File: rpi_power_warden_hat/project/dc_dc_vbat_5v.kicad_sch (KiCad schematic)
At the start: 15 parts, among them U4 TPS563200

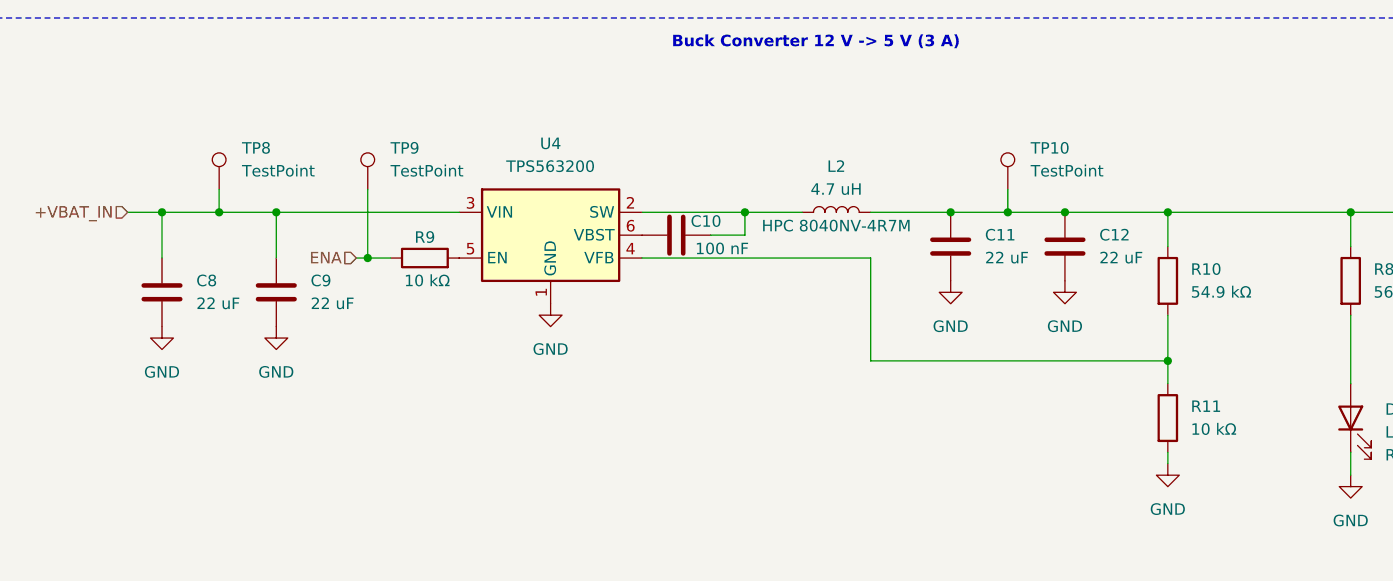
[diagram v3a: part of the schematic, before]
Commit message: add RPi HAT eeprom to schematic
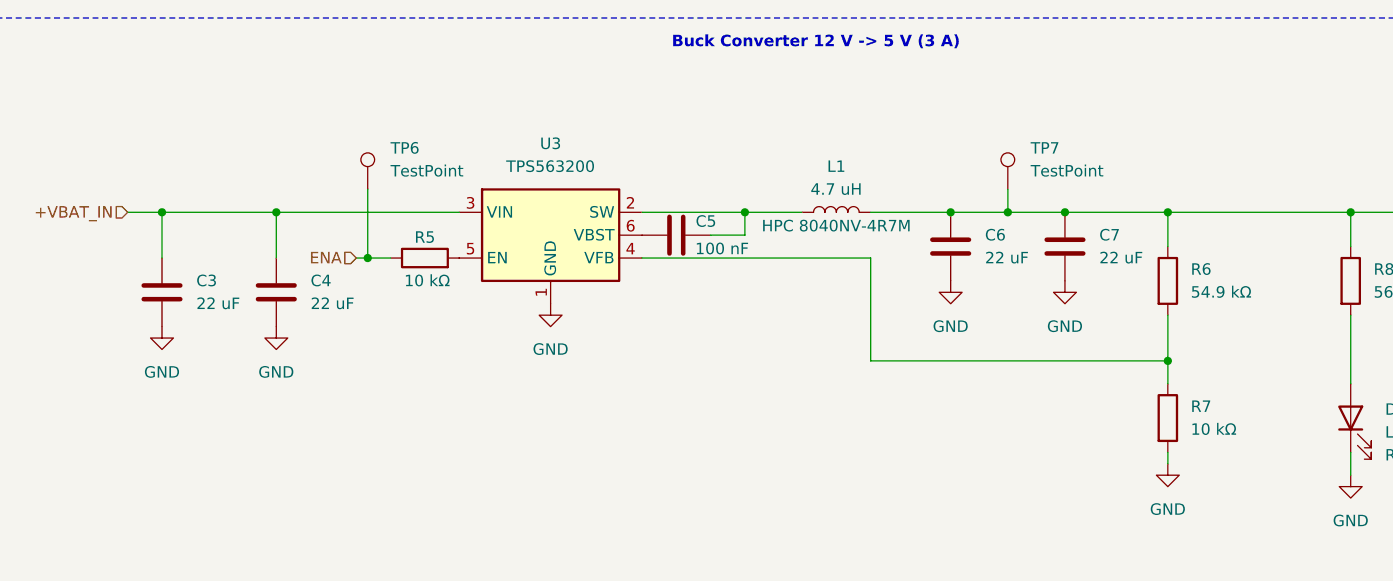
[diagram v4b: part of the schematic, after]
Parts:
- removed TP8: TestPoint, TestPoint:TestPoint_Pad_D2.5mm, symbol Connector:TestPoint
- renumbered C8 to C3, C9 to C4, C10 to C5, C11 to C6, C12 to C7, L2 to L1, R9 to R5, R10 to R6, R11 to R7, TP9 to TP6, TP10 to TP7, U4 to U3
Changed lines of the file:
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@@
 	)
 	(junction
-		(at 91.44 85.09)
-		(diameter 0)
-		(color 0 0 0 0)
-	)
-	(junction
 		(at 107.95 90.17)
 		(diameter 0)
@@
 	(wire
 		(pts
-			(xy 91.44 85.09) (xy 97.79 85.09)
+			(xy 85.09 85.09) (xy 97.79 85.09)
 		)
 		(stroke
@@
 	(wire
 		(pts
-			(xy 91.44 82.55) (xy 91.44 85.09)
-		)
-		(stroke
-			(width 0)
-			(type default)
-		)
-	)
-	(wire
-		(pts
 			(xy 217.17 85.09) (xy 217.17 88.9)
 		)
@@
 	(wire
 		(pts
-			(xy 85.09 85.09) (xy 91.44 85.09)
-		)
-		(stroke
-			(width 0)
-			(type default)
-		)
-	)
-	(wire
-		(pts
 			(xy 138.43 90.17) (xy 163.83 90.17)
 		)
@@
 		(dnp no)
 		(fields_autoplaced yes)
-		(property "Reference" "C8"
+		(property "Reference" "C3"
 			(at 88.9 92.7099 0)
 			(effects
@@
 		(dnp no)
 		(fields_autoplaced yes)
-		(property "Reference" "#PWR24"
+		(property "Reference" "#PWR17"
 			(at 172.72 99.06 0)
 			(effects
@@
 		(dnp no)
 		(fields_autoplaced yes)
-		(property "Reference" "C12"
+		(property "Reference" "C7"
 			(at 189.23 87.6299 0)
 			(effects
@@
 		(dnp no)
 		(fields_autoplaced yes)
-		(property "Reference" "R11"
+		(property "Reference" "R7"
 			(at 199.39 106.6799 0)
 			(effects
@@
 		(dnp no)
 		(fields_autoplaced yes)
-		(property "Reference" "#PWR23"
+		(property "Reference" "#PWR16"
 			(at 128.27 101.6 0)
 			(effects
@@
 		(dnp no)
 		(fields_autoplaced yes)
-		(property "Reference" "TP10"
+		(property "Reference" "TP7"
 			(at 181.61 77.9779 0)
 			(effects
@@
 		(dnp no)
 		(fields_autoplaced yes)
-		(property "Reference" "#PWR25"
+		(property "Reference" "#PWR18"
 			(at 185.42 99.06 0)
 			(effects
@@
 		(on_board yes)
 		(dnp no)
-		(property "Reference" "C10"
+		(property "Reference" "C5"
 			(at 145.542 86.106 90)
 			(effects
@@
 		(dnp no)
 		(fields_autoplaced yes)
-		(property "Reference" "#PWR22"
+		(property "Reference" "#PWR15"
 			(at 97.79 104.14 0)
 			(effects
@@
 	)
 	(symbol
-		(lib_id "Connector:TestPoint")
-		(at 91.44 82.55 0)
-		(unit 1)
-		(exclude_from_sim no)
-		(in_bom yes)
-		(on_board yes)
-		(dnp no)
-		(fields_autoplaced yes)
-		(property "Reference" "TP8"
-			(at 93.98 77.9779 0)
-			(effects
-				(font
-					(size 1.27 1.27)
-				)
-				(justify left)
-			)
-		)
-		(property "Value" "TestPoint"
-			(at 93.98 80.5179 0)
-			(effects
-				(font
-					(size 1.27 1.27)
-				)
-				(justify left)
-			)
-		)
-		(property "Footprint" "TestPoint:TestPoint_Pad_D2.5mm"
-			(at 96.52 82.55 0)
-			(effects
-				(font
-					(size 1.27 1.27)
-				)
-				(hide yes)
-			)
-		)
-		(property "Datasheet" "~"
-			(at 96.52 82.55 0)
-			(effects
-				(font
-					(size 1.27 1.27)
-				)
-				(hide yes)
-			)
-		)
-		(property "Description" "test point"
-			(at 91.44 82.55 0)
-			(effects
-				(font
-					(size 1.27 1.27)
-				)
-				(hide yes)
-			)
-		)
-		(pin "1"
-		)
-		(instances
-			(project "rpi_power_warden_hat"
-				(path "/8692c5de-a943-41e8-8e29-f6c5e99cda34/5bbc6f2d-46db-4213-8835-1ada71ba8330"
-					(reference "TP5")
-					(unit 1)
-				)
-				(path "/8692c5de-a943-41e8-8e29-f6c5e99cda34/cc58a92a-1392-4aa4-91cc-7a70ded8904f"
-					(reference "TP8")
-					(unit 1)
-				)
-			)
-		)
-	)
-	(symbol
 		(lib_id "Device:LED")
 		(at 217.17 107.95 90)
@@
 		(dnp no)
 		(fields_autoplaced yes)
-		(property "Reference" "TP9"
+		(property "Reference" "TP6"
 			(at 110.49 77.9779 0)
 			(effects
@@
 		(dnp no)
 		(fields_autoplaced yes)
-		(property "Reference" "#PWR21"
+		(property "Reference" "#PWR14"
 			(at 85.09 104.14 0)
 			(effects
@@
 		(dnp no)
 		(fields_autoplaced yes)
-		(property "Reference" "C9"
+		(property "Reference" "C4"
 			(at 101.6 92.7099 0)
 			(effects
@@
 		(dnp no)
 		(fields_autoplaced yes)
-		(property "Reference" "#PWR26"
+		(property "Reference" "#PWR19"
 			(at 196.85 119.38 0)
 			(effects
@@
 		(dnp no)
 		(fields_autoplaced yes)
-		(property "Reference" "U4"
+		(property "Reference" "U3"
 			(at 128.27 77.47 0)
 			(effects
@@
 		(dnp no)
 		(fields_autoplaced yes)
-		(property "Reference" "C11"
+		(property "Reference" "C6"
 			(at 176.53 87.6299 0)
 			(effects
@@
 		(dnp no)
 		(fields_autoplaced yes)
-		(property "Reference" "R10"
+		(property "Reference" "R6"
 			(at 199.39 91.4399 0)
 			(effects
@@
 		(on_board yes)
 		(dnp no)
-		(property "Reference" "R9"
+		(property "Reference" "R5"
 			(at 114.3 87.884 90)
 			(effects
@@
 		(on_board yes)
 		(dnp no)
-		(property "Reference" "L2"
+		(property "Reference" "L1"
 			(at 160.02 80.01 90)
 			(effects

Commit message: re-annotate schematic
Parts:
- renumbered C3 to C4, C4 to C5, C5 to C6, C6 to C7, C7 to C8, R7 to R10, R8 to R11, R5 to R8, R6 to R9, U3 to U4

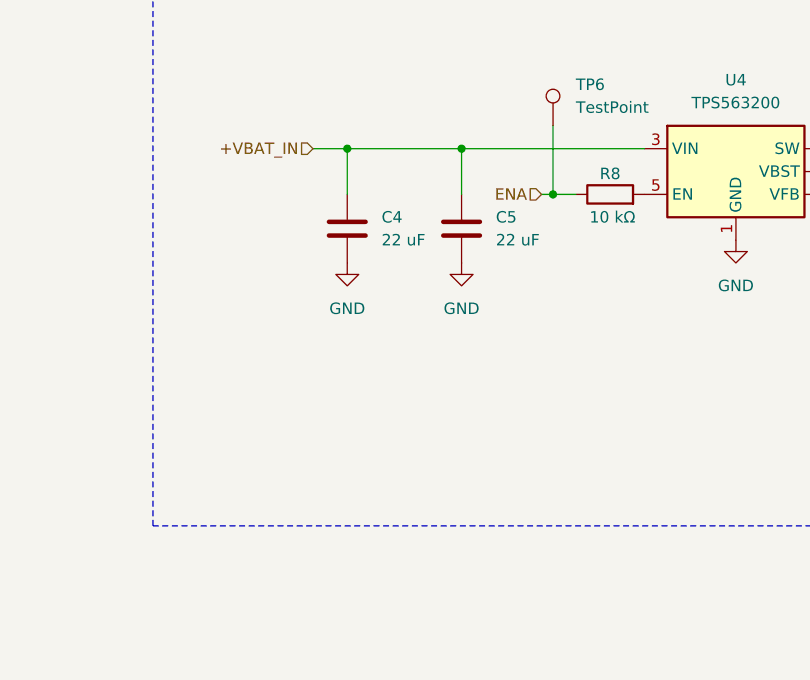
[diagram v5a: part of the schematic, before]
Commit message: add and gate in swiched power supplies enable
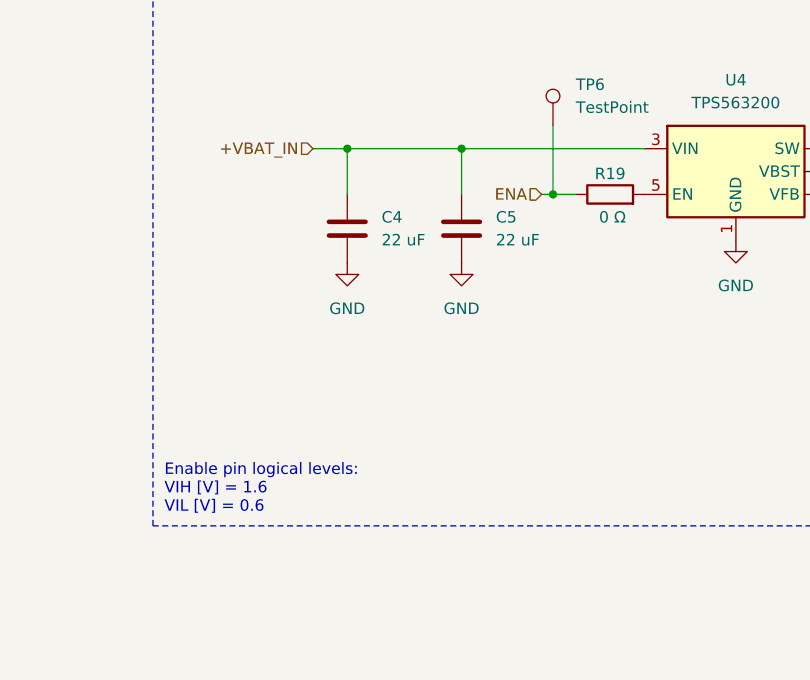
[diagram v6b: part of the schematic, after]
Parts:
- removed R8: 10 kΩ, Resistor_SMD:R_0603_1608Metric_Pad0.98x0.95mm_HandSolder, symbol Device:R
- added R19: 0 Ω, Resistor_SMD:R_0603_1608Metric_Pad0.98x0.95mm_HandSolder, symbol Device:R
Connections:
- net ENA: now also R19.1
- net at U4.5 (EN): now also R19.2
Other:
- note added: "Enable pin logical levels: VIH [V] = 1.6 VIL [V] = 0.6"
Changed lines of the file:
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@@
+		)
+	)
+	(text "Enable pin logical levels:\nVIH [V] = 1.6\nVIL [V] = 0.6"
+		(exclude_from_sim no)
+		(at 64.77 122.936 0)
+		(effects
+			(font
+				(size 1.27 1.27)
+			)
+			(justify left)
 		)
 	)
@@
 	)
 	(symbol
+		(lib_id "Device:R")
+		(at 114.3 90.17 90)
+		(unit 1)
+		(exclude_from_sim no)
+		(in_bom yes)
+		(on_board yes)
+		(dnp no)
+		(property "Reference" "R19"
+			(at 114.3 87.884 90)
+			(effects
+				(font
+					(size 1.27 1.27)
+				)
+			)
+		)
+		(property "Value" "0 Ω"
+			(at 114.554 92.71 90)
+			(effects
+				(font
+					(size 1.27 1.27)
+				)
+			)
+		)
+		(property "Footprint" "Resistor_SMD:R_0603_1608Metric_Pad0.98x0.95mm_HandSolder"
+			(at 114.3 91.948 90)
+			(effects
+				(font
+					(size 1.27 1.27)
+				)
+				(hide yes)
+			)
+		)
+		(property "Datasheet" "~"
+			(at 114.3 90.17 0)
+			(effects
+				(font
+					(size 1.27 1.27)
+				)
+				(hide yes)
+			)
+		)
+		(property "Description" "RES SMD 0 OHM JUMPER 1/10W 0603"
+			(at 114.3 90.17 0)
+			(effects
+				(font
+					(size 1.27 1.27)
+				)
+				(hide yes)
+			)
+		)
+		(property "mpn" "ERJ-3GEY0R00V"
+			(at 114.3 90.17 0)
+			(effects
+				(font
+					(size 1.27 1.27)
+				)
+				(hide yes)
+			)
+		)
+		(property "manufacturer" "Panasonic Electronic Components"
+			(at 114.3 90.17 0)
+			(effects
+				(font
+					(size 1.27 1.27)
+				)
+				(hide yes)
+			)
+		)
+		(pin "1"
+		)
+		(pin "2"
+		)
+		(instances
+			(project "rpi_power_warden_hat"
+				(path "/8692c5de-a943-41e8-8e29-f6c5e99cda34/5bbc6f2d-46db-4213-8835-1ada71ba8330"
+					(reference "R19")
+					(unit 1)
+				)
+				(path "/8692c5de-a943-41e8-8e29-f6c5e99cda34/cc58a92a-1392-4aa4-91cc-7a70ded8904f"
+					(reference "R12")
+					(unit 1)
+				)
+			)
+		)
+	)
+	(symbol
 		(lib_id "Device:C")
 		(at 97.79 93.98 0)
@@
 					(unit 1)
 				)
-			)
-		)
-	)
-	(symbol
-		(lib_id "Device:R")
-		(at 114.3 90.17 90)
-		(unit 1)
-		(exclude_from_sim no)
-		(in_bom yes)
-		(on_board yes)
-		(dnp no)
-		(property "Reference" "R8"
-			(at 114.3 87.884 90)
-			(effects
-				(font
-					(size 1.27 1.27)
-				)
-			)
-		)
-		(property "Value" "10 kΩ"
-			(at 114.554 92.71 90)
-			(effects
-				(font
-					(size 1.27 1.27)
-				)
-			)
-		)
-		(property "Footprint" "Resistor_SMD:R_0603_1608Metric_Pad0.98x0.95mm_HandSolder"
-			(at 114.3 91.948 90)
-			(effects
-				(font
-					(size 1.27 1.27)
-				)
-				(hide yes)
-			)
-		)
-		(property "Datasheet" "~"
-			(at 114.3 90.17 0)
-			(effects
-				(font
-					(size 1.27 1.27)
-				)
-				(hide yes)
-			)
-		)
-		(property "Description" "RES SMD 10K OHM 1% 1/10W"
-			(at 114.3 90.17 0)
-			(effects
-				(font
-					(size 1.27 1.27)
-				)
-				(hide yes)
-			)
-		)
-		(property "mpn" "ERJ-3EKF1002V"
-			(at 114.3 90.17 0)
-			(effects
-				(font
-					(size 1.27 1.27)
-				)
-				(hide yes)
-			)
-		)
-		(property "manufacturer" "Panasonic Electronic Components"
-			(at 114.3 90.17 0)
-			(effects
-				(font
-					(size 1.27 1.27)
-				)
-				(hide yes)
-			)
-		)
-		(pin "1"
-		)
-		(pin "2"
-		)
-		(instances
-			(project "rpi_power_warden_hat"
-				(path "/8692c5de-a943-41e8-8e29-f6c5e99cda34/5bbc6f2d-46db-4213-8835-1ada71ba8330"
-					(reference "R8")
-					(unit 1)
-				)
-				(path "/8692c5de-a943-41e8-8e29-f6c5e99cda34/cc58a92a-1392-4aa4-91cc-7a70ded8904f"
-					(reference "R12")
-					(unit 1)
-				)
